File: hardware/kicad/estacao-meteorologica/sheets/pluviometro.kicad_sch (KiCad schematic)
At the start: 12 parts, among them J30 R-RJ11R06P-A800, U30 SN74LVC1G17DBVR

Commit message: refatoracao: atualizacoes de hardware e falta revisao LoRa
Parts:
- added R32: 1k, Resistor_SMD:R_0603_1608Metric, symbol Device:R
- J30: Function RJ11 individual; contatos centrais -> Conector do pluviometro; reed externo entre p3 e p4; Rating 6P6C; p3=return; p4=signal; THT -> 6P6C; p3=+3V3 via R32; p4=sinal; THT
- R30: Function Pull-up ANTES do resistor serie; reed fechado ~0V -> Pull-down do sinal bruto; reed aberto = nivel baixo
- U30: Function Schmitt nao inversor; reed fecha -> borda de descida -> Schmitt nao inversor; reed fecha -> borda de subida em RAIN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
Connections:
- net +3V3: now also R32.1; no longer R30.1
- net GND: now also R30.1; no longer J30.3
- new net: J30.3, R32.2
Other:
- note added: "R32=1k fornece +3V3 ao p3; R30=10k e o pull-down do p4. Reed aberto = 0 V; fechado = ~3,0 V e saida alta. C30=100n: tau de subida ~0,56 ms e de descida ~1,47 ms. PENDENCIA DE FIRMWARE: usar EXTI na subida e sem pull interno; o codigo atual ainda usa descida com pull-up."
- note removed: "Pull-up no lado do cabo evita divisor 4k7/10k na entrada Schmitt. Tau abertura=1,47 ms; fechamento=0,47 ms. Debounce atual: 200 ms."
- moved on the sheet: R30

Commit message: refatoracao: lora + Verificacao projeto inteiro
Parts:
- C30, C31: Modelo 3D (none) -> ${KICAD9_3DMODEL_DIR}/Capacitor_SMD.3dshapes/C_0603_1608Met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; Status_Ficha (none) -> Conferido no catalogo em 2026-09-24; verificar estoque ao c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
- D30: Modelo 3D (none) -> ${KICAD9_3DMODEL_DIR}/Diode_SMD.3dshapes/D_SOD-882.step; Status_Ficha (none) -> Conferido no catalogo em 2026-09-24; verificar estoque ao c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
- D31: Modelo 3D (none) -> ${KICAD9_3DMODEL_DIR}/Package_TO_SOT_SMD.3dshapes/SOT-23.st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; Status_Ficha (none) -> Conferido no catalogo em 2026-09-24; verificar estoque ao c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
- J30: Manufacturer Ckmtw -> Ckmtw(Shenzhen Cankemeng); Modelo 3D (none) -> ${KIPRJMOD}/../../libraries/Sensores_Meteo/Sensores_Meteo.3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; Status_Ficha (none) -> Conferido no catalogo em 2026-09-24; verificar estoque ao c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
- R30, R31: Manufacturer UNI-ROYAL -> UNI-ROYAL(Uniroyal Elec); Modelo 3D (none) -> ${KICAD9_3DMODEL_DIR}/Resistor_SMD.3dshapes/R_0603_1608Metr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; Status_Ficha (none) -> Conferido no catalogo em 2026-09-24; verificar estoque ao c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
- R32: LCSC C25804 -> C21190; LCSC Part C25804 -> C21190; MPN 0603WAF1002T5E -> 0603WAF1001T5E; Manufacturer UNI-ROYAL -> UNI-ROYAL(Uniroyal Elec); Modelo 3D (none) -> ${KICAD9_3DMODEL_DIR}/Resistor_SMD.3dshapes/R_0603_1608Metr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; Status_Ficha (none) -> Conferido no catalogo em 2026-09-24; verificar estoque ao c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
- TP30, TP31, TP32, TP33: LCSC (none) -> N/A; LCSC Part (none) -> N/A; MPN (none) -> N/A - elemento de cobre da PCB; Manufacturer (none) -> N/A; Modelo 3D (none) -> N/A - geometria de cobre, sem corpo
- U30: Modelo 3D (none) -> ${KICAD9_3DMODEL_DIR}/Package_TO_SOT_SMD.3dshapes/SOT-23-5.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; Status_Ficha (none) -> Conferido no catalogo em 2026-09-24; verificar estoque ao c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
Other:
- moved on the sheet: TP32

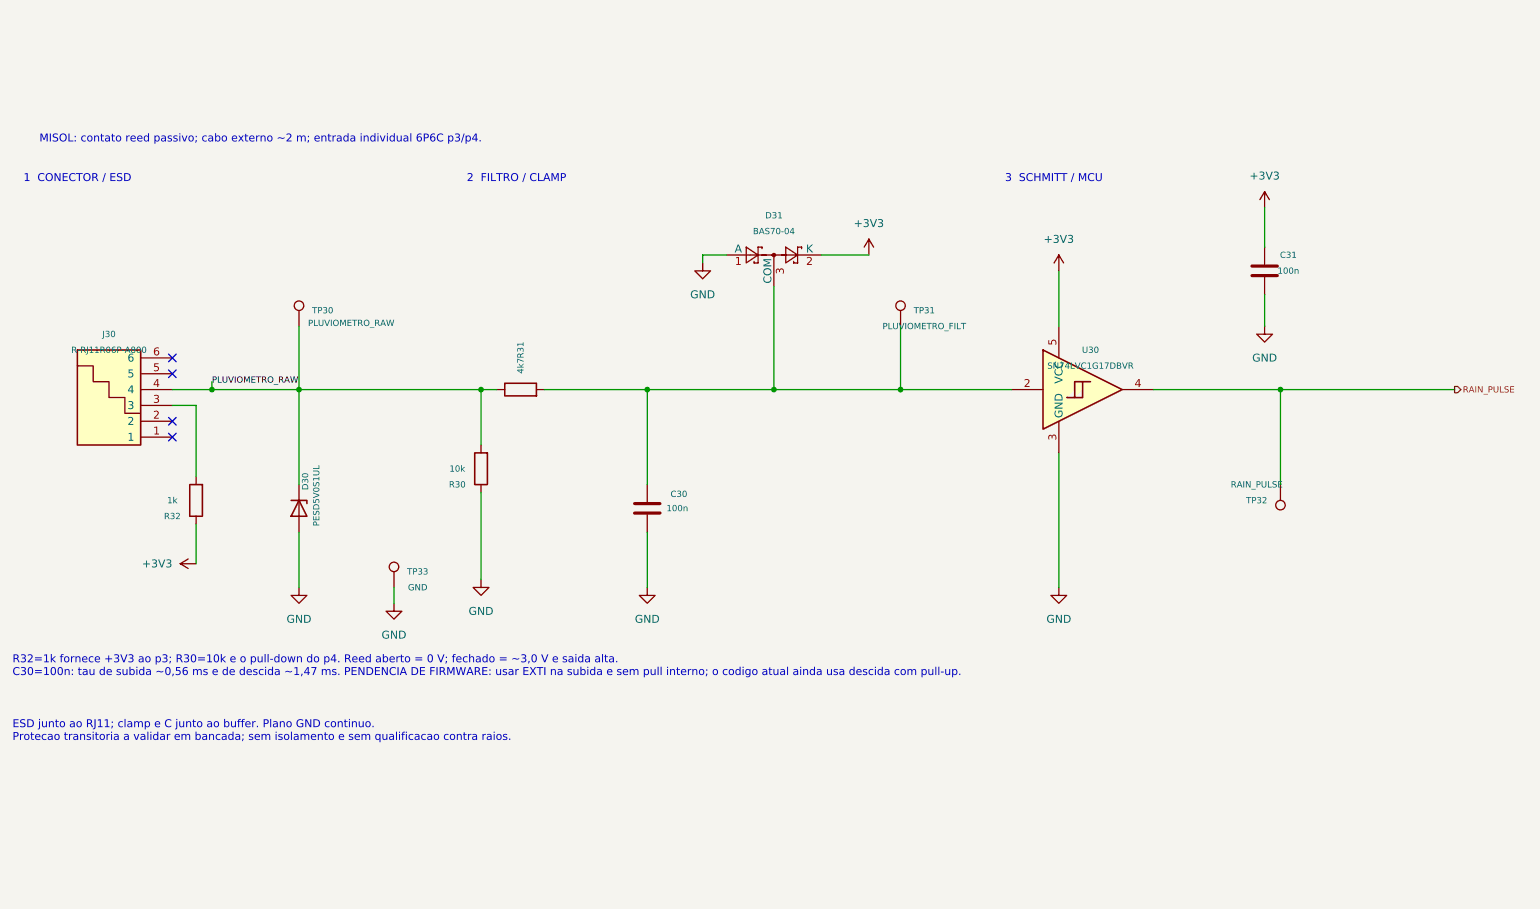
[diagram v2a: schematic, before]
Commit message: Padronizacao de nomes e numero de componentes
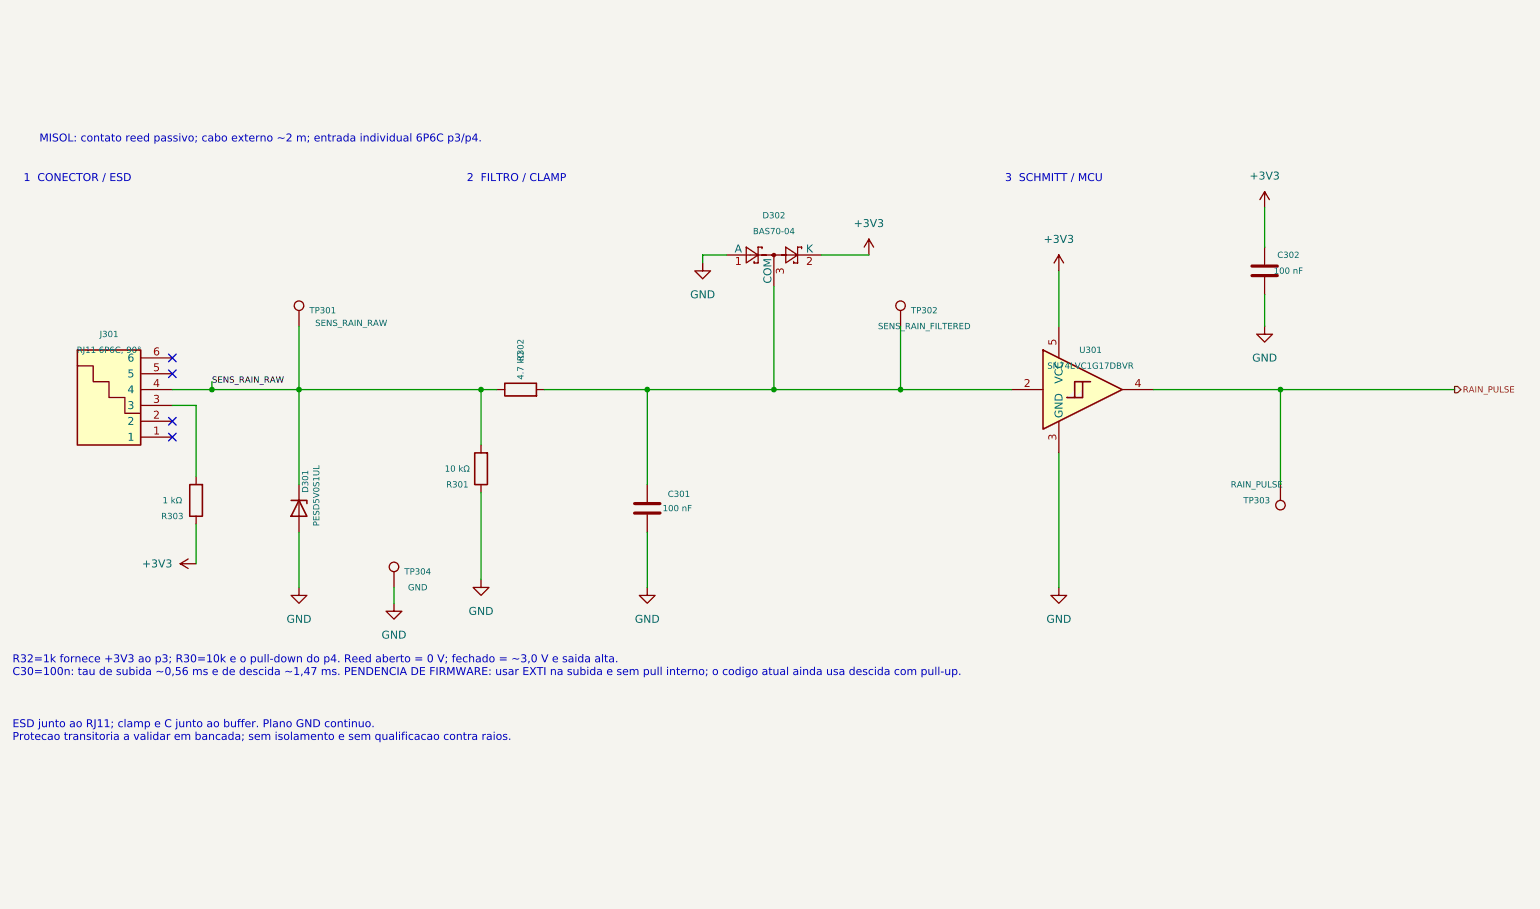
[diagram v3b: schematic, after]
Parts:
- C301: renamed from C30; value 100n -> 100 nF; Assembly (none) -> SMT; LCSC Part C14663 -> (none); Modelo 3D ${KICAD9_3DMODEL_DIR}/Capacitor_SMD.3dshapes/C_0603_1608Met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 -> (none); Rating 10%; 50V; X7R -> (none); Specification (none) -> 10%; 50V; X7R; Status_Ficha Conferido no catalogo em 2026-09-24; verificar estoque ao c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 -> (none); Verification (none) -> Conferido no catalogo em 2026-09-24; verificar estoque ao c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
- C302: renamed from C31; value 100n -> 100 nF; Assembly (none) -> SMT; LCSC Part C14663 -> (none); Modelo 3D ${KICAD9_3DMODEL_DIR}/Capacitor_SMD.3dshapes/C_0603_1608Met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 -> (none); Rating 10%; 50V; X7R -> (none); Specification (none) -> 10%; 50V; X7R; Status_Ficha Conferido no catalogo em 2026-09-24; verificar estoque ao c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 -> (none); Verification (none) -> Conferido no catalogo em 2026-09-24; verificar estoque ao c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
- D301: renamed from D30; Assembly (none) -> SMT; LCSC Part C85402 -> (none); Modelo 3D ${KICAD9_3DMODEL_DIR}/Diode_SMD.3dshapes/D_SOD-882.step -> (none); Rating VRWM=5V; IR max 1uA at 5V/25C; see datasheet -> (none); Specification (none) -> VRWM=5V; IR max 1uA at 5V/25C; see datasheet; Status_Ficha Conferido no catalogo em 2026-09-24; verificar estoque ao c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 -> (none); Verification (none) -> Conferido no catalogo em 2026-09-24; verificar estoque ao c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
- D302: renamed from D31; Assembly (none) -> SMT; LCSC Part C389351 -> (none); Modelo 3D ${KICAD9_3DMODEL_DIR}/Package_TO_SOT_SMD.3dshapes/SOT-23.st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 -> (none); Rating IR max 100nA at 50V/25C; 1=GND, 2=3V3, 3=signal -> (none); Specification (none) -> IR max 100nA at 50V/25C; 1=GND, 2=3V3, 3=signal; Status_Ficha Conferido no catalogo em 2026-09-24; verificar estoque ao c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 -> (none); Verification (none) -> Conferido no catalogo em 2026-09-24; verificar estoque ao c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
- J301: renamed from J30; value R-RJ11R06P-A800 -> RJ11 6P6C, 90°; Assembly (none) -> SMT; LCSC Part C189750 -> (none); Modelo 3D ${KIPRJMOD}/../../libraries/Sensores_Meteo/Sensores_Meteo.3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 -> (none); Rating 6P6C; p3=+3V3 via R32; p4=sinal; THT -> (none); Specification (none) -> 6P6C; p3=+3V3 via R32; p4=sinal; THT; Status_Ficha Conferido no catalogo em 2026-09-24; verificar estoque ao c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 -> (none); Verification (none) -> Conferido no catalogo em 2026-09-24; verificar estoque ao c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
- R301: renamed from R30; value 10k -> 10 kΩ; Assembly (none) -> SMT; LCSC Part C25804 -> (none); Modelo 3D ${KICAD9_3DMODEL_DIR}/Resistor_SMD.3dshapes/R_0603_1608Metr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 -> (none); Rating 1%; 0.1W; 75V -> (none); Specification (none) -> 1%; 0.1W; 75V; Status_Ficha Conferido no catalogo em 2026-09-24; verificar estoque ao c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 -> (none); Verification (none) -> Conferido no catalogo em 2026-09-24; verificar estoque ao c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
- R302: renamed from R31; value 4k7 -> 4.7 kΩ; Assembly (none) -> SMT; LCSC Part C23162 -> (none); Modelo 3D ${KICAD9_3DMODEL_DIR}/Resistor_SMD.3dshapes/R_0603_1608Metr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 -> (none); Rating 1%; 0.1W; 75V -> (none); Specification (none) -> 1%; 0.1W; 75V; Status_Ficha Conferido no catalogo em 2026-09-24; verificar estoque ao c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 -> (none); Verification (none) -> Conferido no catalogo em 2026-09-24; verificar estoque ao c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
- R303: renamed from R32; value 1k -> 1 kΩ; Assembly (none) -> SMT; LCSC Part C21190 -> (none); Modelo 3D ${KICAD9_3DMODEL_DIR}/Resistor_SMD.3dshapes/R_0603_1608Metr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 -> (none); Rating 1%; 0.1W; 75V -> (none); Specification (none) -> 1%; 0.1W; 75V; Status_Ficha Conferido no catalogo em 2026-09-24; verificar estoque ao c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 -> (none); Verification (none) -> Conferido no catalogo em 2026-09-24; verificar estoque ao c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
- TP301: renamed from TP30; value PLUVIOMETRO_RAW -> SENS_RAIN_RAW; Assembly (none) -> PCB — sem compra; Function PLUVIOMETRO_RAW -> SENS_RAIN_RAW; LCSC Part N/A -> (none); Modelo 3D N/A - geometria de cobre, sem corpo -> (none); Rating Copper pad; no purchased component -> (none); Specification (none) -> Copper pad; no purchased component
- TP302: renamed from TP31; value PLUVIOMETRO_FILT -> SENS_RAIN_FILTERED; Assembly (none) -> PCB — sem compra; Function PLUVIOMETRO_FILT -> SENS_RAIN_FILTERED; LCSC Part N/A -> (none); Modelo 3D N/A - geometria de cobre, sem corpo -> (none); Rating Copper pad; no purchased component -> (none); Specification (none) -> Copper pad; no purchased component
- TP303: renamed from TP32; Assembly (none) -> PCB — sem compra; LCSC Part N/A -> (none); Modelo 3D N/A - geometria de cobre, sem corpo -> (none); Rating Copper pad; no purchased component -> (none); Specification (none) -> Copper pad; no purchased component
- TP304: renamed from TP33; Assembly (none) -> PCB — sem compra; LCSC Part N/A -> (none); Modelo 3D N/A - geometria de cobre, sem corpo -> (none); Rating Copper pad; no purchased component -> (none); Specification (none) -> Copper pad; no purchased component
- U301: renamed from U30; Assembly (none) -> SMT; LCSC Part C7836 -> (none); Modelo 3D ${KICAD9_3DMODEL_DIR}/Package_TO_SOT_SMD.3dshapes/SOT-23-5.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 -> (none); Rating Non-inverting Schmitt; 1=NC 2=A 3=GND 4=Y 5=VCC -> (none); Specification (none) -> Non-inverting Schmitt; 1=NC 2=A 3=GND 4=Y 5=VCC; Status_Ficha Conferido no catalogo em 2026-09-24; verificar estoque ao c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 -> (none); Verification (none) -> Conferido no catalogo em 2026-09-24; verificar estoque ao c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
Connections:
- net PLUVIOMETRO_RAW renamed SENS_RAIN_RAW

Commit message: Add test points necessarios para debug
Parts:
- TP301, TP302, TP303: footprint TestPoint:TestPoint_Pad_D1.5mm -> TestPoint:TestPoint_Pad_D1.0mm
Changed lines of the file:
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@@
 			)
 		)
-		(property "Footprint" "TestPoint:TestPoint_Pad_D1.5mm"
+		(property "Footprint" "TestPoint:TestPoint_Pad_D1.0mm"
 			(at 223.52 95.25 0)
 			(effects
@@
 			)
 		)
-		(property "Description" "Ponto de teste em cobre, pad circular de 1,5 mm; rede RAIN_PULSE"
+		(property "Description" "Ponto de teste em cobre, pad circular de 1,0 mm; rede RAIN_PULSE"
 			(at 223.52 95.25 0)
 			(effects
@@
 			)
 		)
-		(property "Footprint" "TestPoint:TestPoint_Pad_D1.5mm"
+		(property "Footprint" "TestPoint:TestPoint_Pad_D1.0mm"
 			(at 162.56 69.85 0)
 			(effects
@@
 			)
 		)
-		(property "Description" "Ponto de teste em cobre, pad circular de 1,5 mm; rede PLUVIOMETRO_FILT"
+		(property "Description" "Ponto de teste em cobre, pad circular de 1,0 mm; rede PLUVIOMETRO_FILT"
 			(at 162.56 69.85 0)
 			(effects
@@
 			)
 		)
-		(property "Footprint" "TestPoint:TestPoint_Pad_D1.5mm"
+		(property "Footprint" "TestPoint:TestPoint_Pad_D1.0mm"
 			(at 66.04 69.85 0)
 			(effects
@@
 			)
 		)
-		(property "Description" "Ponto de teste em cobre, pad circular de 1,5 mm; rede PLUVIOMETRO_RAW"
+		(property "Description" "Ponto de teste em cobre, pad circular de 1,0 mm; rede PLUVIOMETRO_RAW"
 			(at 66.04 69.85 0)
 			(effects

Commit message: feat(hardware): consolida revisão PCB V2
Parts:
- TP304: footprint TestPoint:TestPoint_Pad_D1.5mm -> TestPoint:TestPoint_Pad_D1.0mm
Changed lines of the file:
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@@
 			)
 		)
-		(property "Footprint" "TestPoint:TestPoint_Pad_D1.5mm"
+		(property "Footprint" "TestPoint:TestPoint_Pad_D1.0mm"
 			(at 81.28 111.76 0)
 			(effects
